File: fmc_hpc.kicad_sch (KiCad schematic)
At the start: 30 parts, among them J5 ASP-134486-01

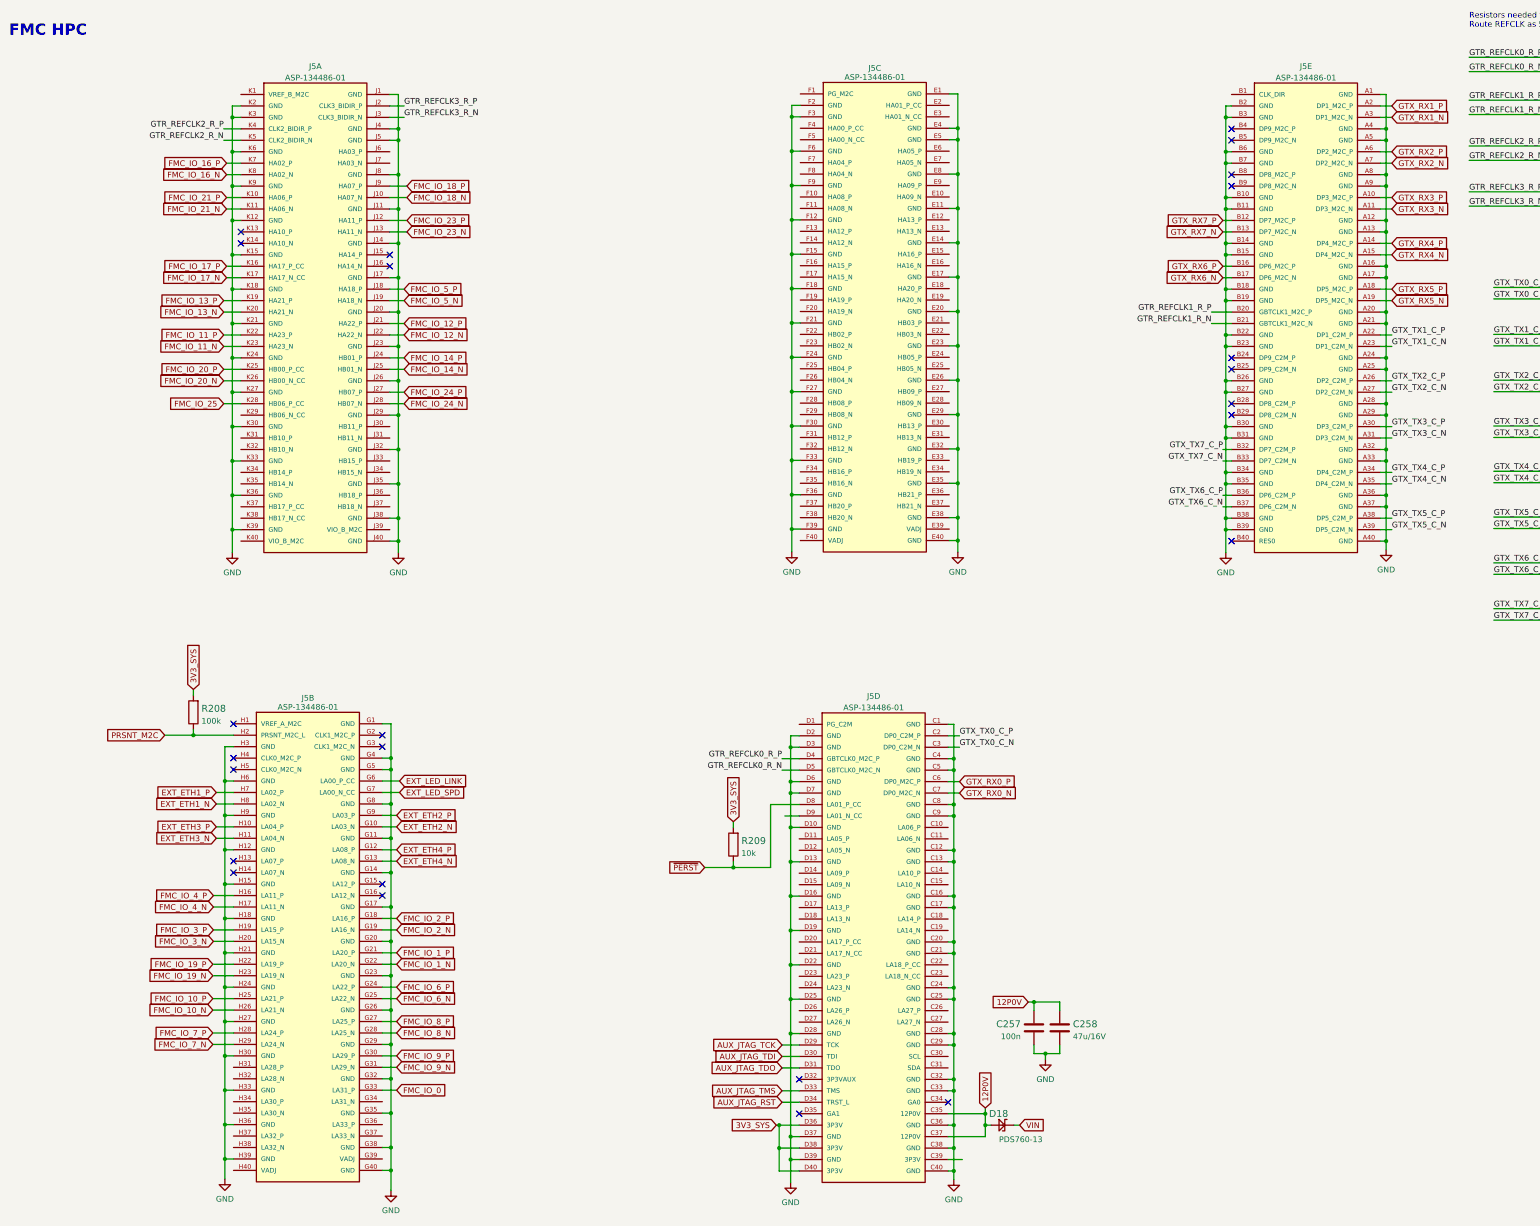
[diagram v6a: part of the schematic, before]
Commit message: Implement all review fixes, route control signals from FMC to FPGA
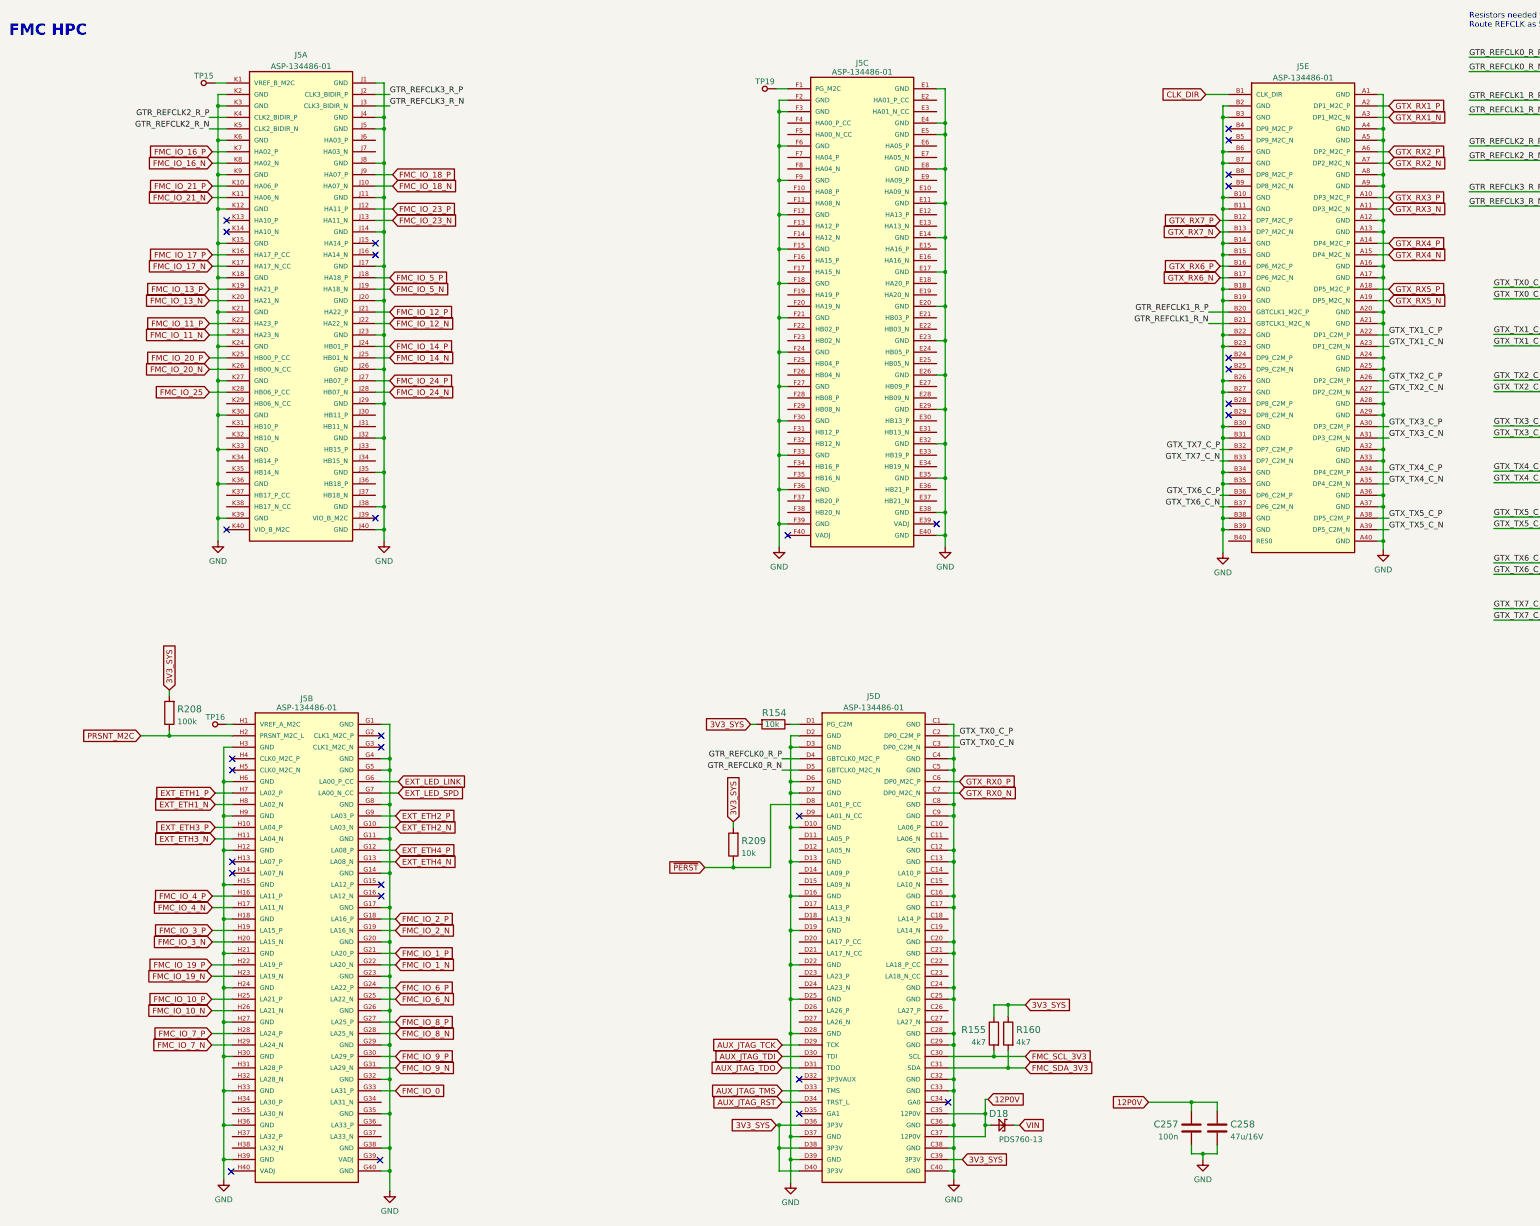
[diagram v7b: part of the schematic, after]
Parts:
- added R154: R_10k_0402, antmicro-footprints:0402-res, symbol antmicroResistors0402:R_10k_0402
- added R155, R160: R_4k7_0402, data-center-dram-tester-footprints:0402-res, symbol data-center-dram-tester:R_4k7_0402
- added TP15, TP16, TP19: TP_SMD_0_75MM, antmicro-footprints:Testpoint_smd_0_75mm, symbol antmicroTestPoints:TP_SMD_0_75MM
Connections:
- net 3V3_SYS: now also J5.C39 (3P3V), R154.2, R155.1, R160.1
- net at J5.H1 (VREF_A_M2C): now also TP16.1
- net CLK_DIR: now reaches J5.B1 (CLK_DIR)
- net at J5.F1 (PG_M2C): now also TP19.1
- net at J5.K1 (VREF_B_M2C): now also TP15.1
- net FMC_SCL_3V3: now reaches J5.C30 (SCL)
- net FMC_SCL_3V3: now also R155.2
- net FMC_SDA_3V3: now reaches J5.C31 (SDA)
- net FMC_SDA_3V3: now also R160.2
- net at J5.D1 (PG_C2M): now also R154.1
- no-connect marks 25 -> 30
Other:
- moved on the sheet: C257, C258, J5A, J5C, J5E, R208
